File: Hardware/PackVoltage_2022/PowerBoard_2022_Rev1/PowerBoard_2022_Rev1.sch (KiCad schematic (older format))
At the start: 0 parts

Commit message: 12V stuff and hierarchical tags
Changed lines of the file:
@@
 $Descr A4 11693 8268
 encoding utf-8
-Sheet 1 8
+Sheet 1 10
 Title ""
 Date ""
@@
 $EndDescr
 $Sheet
-S 9350 850  1350 1100
+S 9750 650  1350 1100
 U 61563C60
 F0 "Bucks" 50
 F1 "Bucks.sch" 50
-F2 "PV" I L 9350 900 50
-F3 "5V" I L 9350 1000 50
-F4 "3.3V" I L 9350 1100 50
-F5 "12V" I L 9350 1200 50
-F6 "12VA" I L 9350 1300 50
+F2 "PV" I L 9750 700 50
+F3 "5V" I L 9750 800 50
+F4 "3.3V" I L 9750 900 50
+F5 "12V" I L 9750 1000 50
+F6 "12VA" I L 9750 1100 50
 $EndSheet
 $Sheet
@@
 $EndSheet
 $Sheet
-S 4800 3700 2650 2100
+S 4750 3700 2650 2100
 U 615E92DD
 F0 "ANDERSONS" 50
 F1 "andersons.sch" 50
-F2 "Anderson_M2" I L 4800 3900 50
-F3 "Anderson_M1" I L 4800 3800 50
-F4 "Anderson_M3" I L 4800 4000 50
-F5 "Anderson_M4" I L 4800 4100 50
-F6 "Anderson_M5" I L 4800 4200 50
-F7 "Anderson_M6" I L 4800 4300 50
-F8 "Anderson_M7" I L 4800 4400 50
+F2 "Anderson_M2" I L 4750 3900 50
+F3 "Anderson_M1" I L 4750 3800 50
+F4 "Anderson_M3" I L 4750 4000 50
+F5 "Anderson_M4" I L 4750 4100 50
+F6 "Anderson_M5" I L 4750 4200 50
+F7 "Anderson_M6" I L 4750 4300 50
+F8 "Anderson_M7" I L 4750 4400 50
+F9 "Anderson_Drive" I L 4750 4500 50
+F10 "Anderson_Aux" I L 4750 4600 50
+F11 "Anderson_Multimedia" I L 4750 4700 50
+F12 "Anderson_SciHeater" I L 4750 4800 50
+F13 "Anderson_POE" I L 4750 4900 50
+F14 "Anderson_SciSensor" I R 7400 3800 50
+F15 "Anderson_BBB" I R 7400 3900 50
+F16 "Anderson_Nav" I R 7400 4000 50
+F17 "Anderson_Cam1" I R 7400 4100 50
+F18 "Anderson_Cam2" I R 7400 4200 50
+F19 "Anderson_Gimbal" I R 7400 4300 50
+F20 "Anderson_NetSwitch" I R 7400 4400 50
 $EndSheet
 $Sheet
-S 1450 3650 2600 2100
+S 850  5200 1450 1450
 U 615D5992
 F0 "MOTORS" 50
 F1 "MOTORS.sch" 50
-F2 "PV" I L 1450 3700 50
-F3 "5V" I L 1450 3800 50
-F4 "Anderson_M1" I L 1450 4900 50
-F5 "Driver_M1" I R 4050 3750 50
-F6 "Current_Sensor_M1" I R 4050 4900 50
+F2 "PV" I L 850 5250 50
+F3 "5V" I L 850 5350 50
+F4 "Anderson_M1" I L 850 6550 50
+F5 "Driver_M1" I R 2300 5250 50
+F6 "Current_Sensor_M1" I R 2300 6550 50
+F7 "Anderson_M2" I L 850 6450 50
+F8 "Driver_M2" I R 2300 5350 50
+F9 "Current_Sensor_M2" I R 2300 6450 50
+F10 "Anderson_M3" I L 850 6350 50
+F11 "Driver_M3" I R 2300 5450 50
+F12 "Current_Sensor_M3" I R 2300 6350 50
+F13 "Anderson_M4" I L 850 6250 50
+F14 "Driver_M4" I R 2300 5550 50
+F15 "Current_Sensor_M4" I R 2300 6250 50
+F16 "Anderson_M5" I L 850 6150 50
+F17 "Driver_M5" I R 2300 5650 50
+F18 "Current_Sensor_M5" I R 2300 6150 50
+F19 "Anderson_M7" I L 850 5950 50
+F20 "Driver_M7" I R 2300 5850 50
+F21 "Current_Sensor_M7" I R 2300 5950 50
+F22 "Anderson_M6" I L 850 6050 50
+F23 "Driver_M6" I R 2300 5750 50
+F24 "Current_Sensor_M6" I R 2300 6050 50
 $EndSheet
 $Sheet
-S 4800 1150 2850 2200
+S 4850 1000 2850 2200
 U 615D7BA0
 F0 "12V" 50
 F1 "12V.sch" 50
+F2 "Anderson_Aux" I L 4850 1100 50
+F3 "PV" I R 7700 1050 50
+F4 "5V" I R 7700 1150 50
+F5 "Anderson_Spare" I L 4850 1200 50
+F6 "Anderson_Nav" I L 4850 1300 50
+F7 "Anderson_SciSensor" I L 4850 1400 50
+F8 "Anderson_BBB" I L 4850 1500 50
+F9 "Anderson_Cam1" I L 4850 1600 50
+F10 "Anderson_Cam2" I L 4850 1700 50
+F11 "Anderson_NetSwitch" I L 4850 1800 50
+F12 "Anderson_Gimbal" I L 4850 1900 50
+F13 "12V" I R 7700 1250 50
+F14 "Driver_Nav" I R 7700 2350 50
+F15 "Driver_SciSensor" I R 7700 2450 50
+F16 "Driver_BBB" I R 7700 2550 50
+F17 "Driver_Cam1" I R 7700 2650 50
+F18 "Driver_Cam2" I R 7700 2750 50
+F19 "Driver_NetSwitch" I R 7700 2850 50
+F20 "Driver_Gimbal" I R 7700 2950 50
+F21 "Driver_Aux" I R 7700 3050 50
+F22 "Driver_Spare" I R 7700 3150 50
+F23 "Current_Sensor_BBB" I L 4850 2350 50
+F24 "Current_Sensor_Nav" I L 4850 2450 50
+F25 "Current_Sensor_SciSensor" I L 4850 2550 50
+F26 "Current_Sensor_Cam1" I L 4850 2650 50
+F27 "Current_Sensor_Cam2" I L 4850 2750 50
+F28 "Current_Sensor_NetSwitch" I L 4850 2850 50
+F29 "Current_Sensor_Gimbal" I L 4850 2950 50
+F30 "Current_Sensor_Aux" I L 4850 3050 50
+F31 "Current_Sensor_Spare" I L 4850 3150 50
 $EndSheet
+$Sheet
+S 2400 3700 2050 1350
+U 61609A41
+F0 "PACK_OTHERS" 50
+F1 "PACK_OTHERS.sch" 50
+F2 "PV" I L 2400 3750 50
+F3 "5V" I L 2400 3850 50
+F4 "Anderson_Drive" I L 2400 4950 50
+F5 "Driver_Drive" I R 4450 3800 50
+F6 "Current_Sensor_Drive" I R 4450 4950 50
+F7 "Anderson_Aux" I L 2400 4850 50
+F8 "Driver_Aux" I R 4450 3900 50
+F9 "Current_Sensor_Aux" I R 4450 4850 50
+F10 "Anderson_SciHeater" I L 2400 4750 50
+F11 "Driver_SciHeater" I R 4450 4000 50
+F12 "Current_Sensor_SciHeater" I R 4450 4750 50
+F13 "Anderson_Multimedia" I L 2400 4650 50
+F14 "Driver_Multimedia" I R 4450 4100 50
+F15 "Current_Sensor_Multimedia" I R 4450 4650 50
+F16 "Anderson_POE" I L 2400 4550 50
+F17 "Driver_POE" I R 4450 4200 50
+F18 "Current_Sensor_POE" I R 4450 4550 50
+$EndSheet
+Text GLabel 9650 700  0    50   Input ~ 0
+PV
+Wire Wire Line
+	9650 700  9750 700
+Text GLabel 7800 1050 2    50   Input ~ 0
+PV
+Wire Wire Line
+	7800 1050 7700 1050
+Text GLabel 2300 3750 0    50   Input ~ 0
+PV
+Wire Wire Line
+	2300 3750 2400 3750
+Text GLabel 750  5250 0    50   Input ~ 0
+PV
+Wire Wire Line
+	750  5250 850  5250
 $EndSCHEMATC

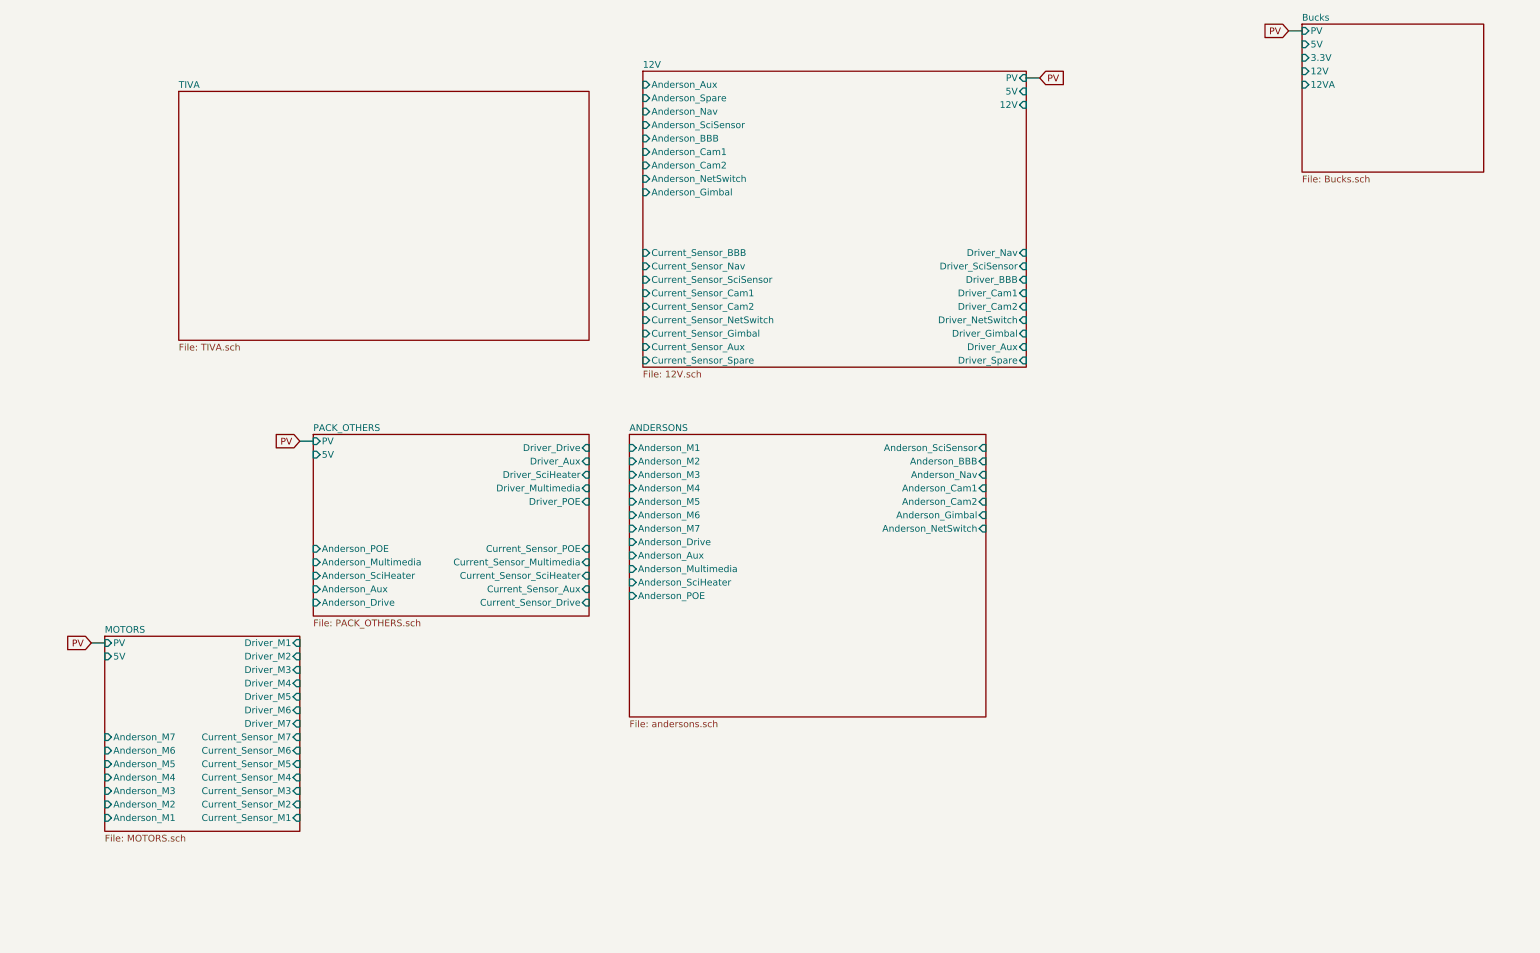
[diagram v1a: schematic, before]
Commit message: Created global tags in main sheet
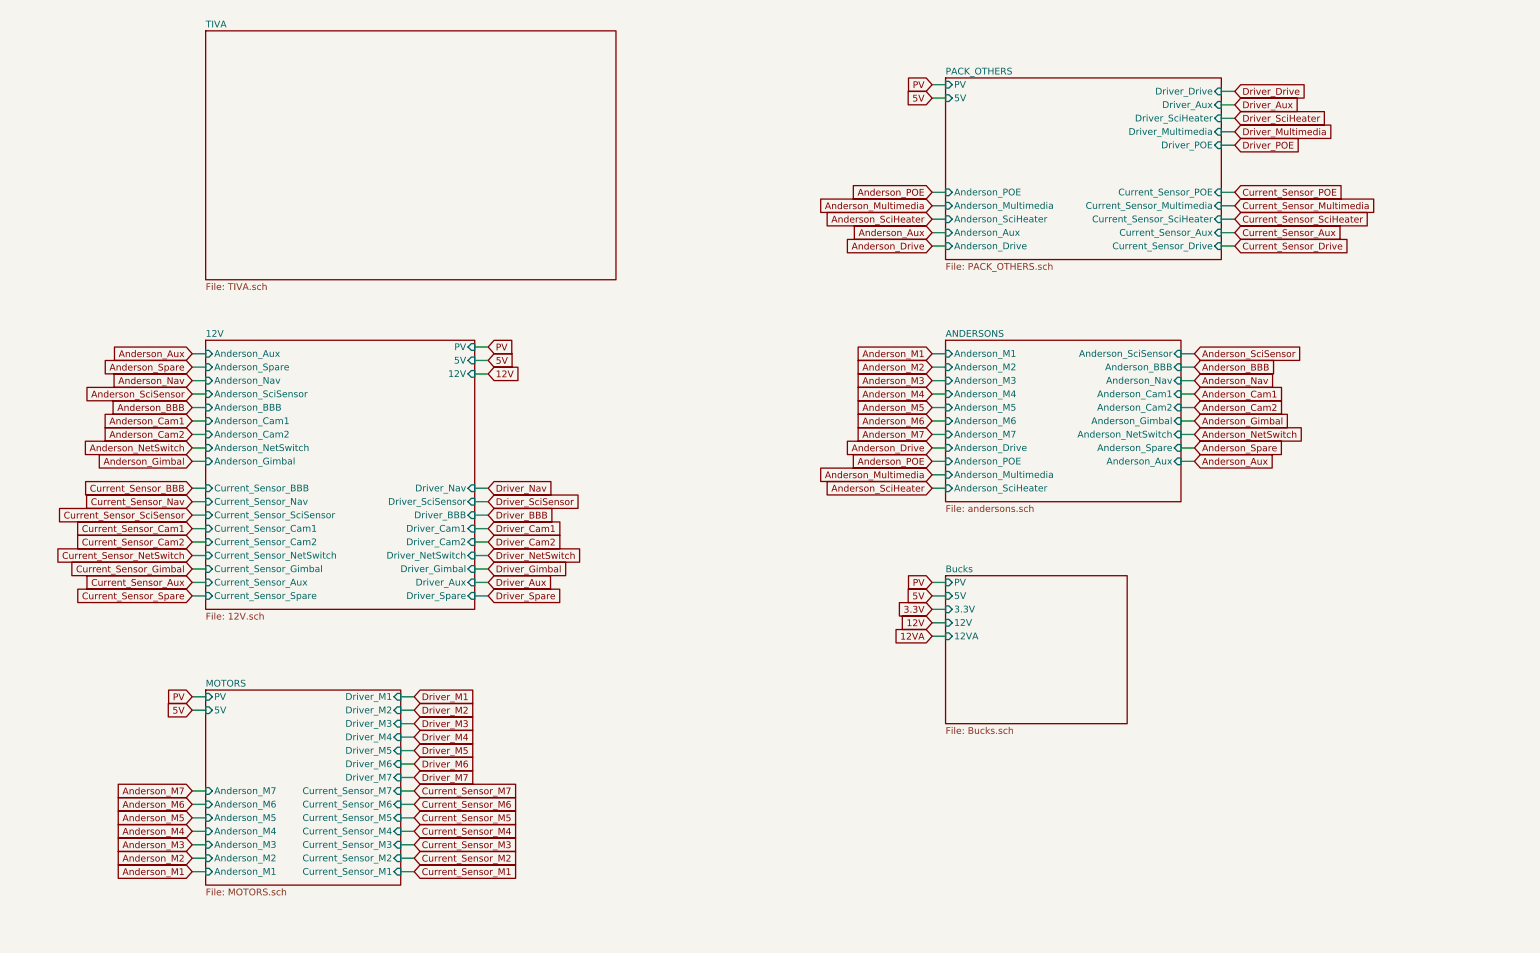
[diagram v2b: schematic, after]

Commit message: TIVA and fixed 12V
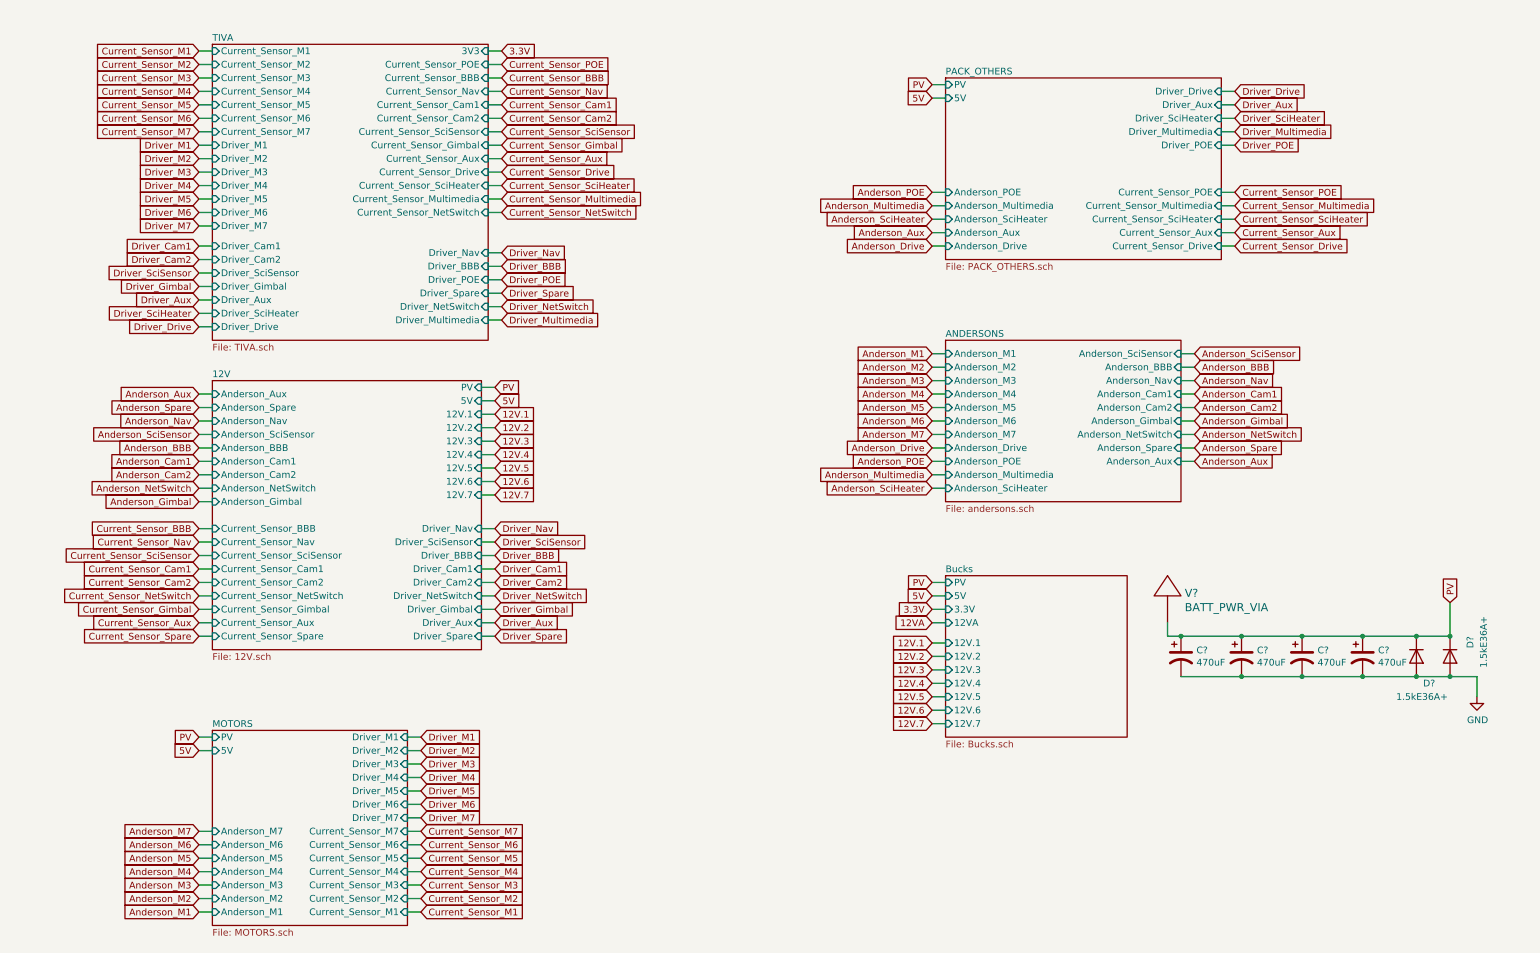
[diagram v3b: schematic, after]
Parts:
- added C? (x4): 470uF, symbol Device:CP1
- added D? (x2): 1.5kE36A+, symbol Device:D
- added V?: BATT_PWR_VIA, symbol MRDT_Drill_Holes:BATT_PWR_VIA
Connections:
- net PV: now also C?.1, C?.1, C?.1, C?.1, D?.1 (K), D?.1 (K), V?.1
- new net GND: C?.2, C?.2, C?.2, C?.2, D?.2 (A), D?.2 (A)

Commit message: Fixed some stuff
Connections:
- net labels added: 12VBBB, 12VCam1, 12VCam2, 12VDrive, 12VGimbal, 12VMultimedia, 12VNav, 12VNetSwitch, 12VSciSensor
- net labels removed: 12V.1, 12V.2, 12V.3, 12V.4, 12V.5, 12V.6, 12V.7
- wire segments 162 -> 160

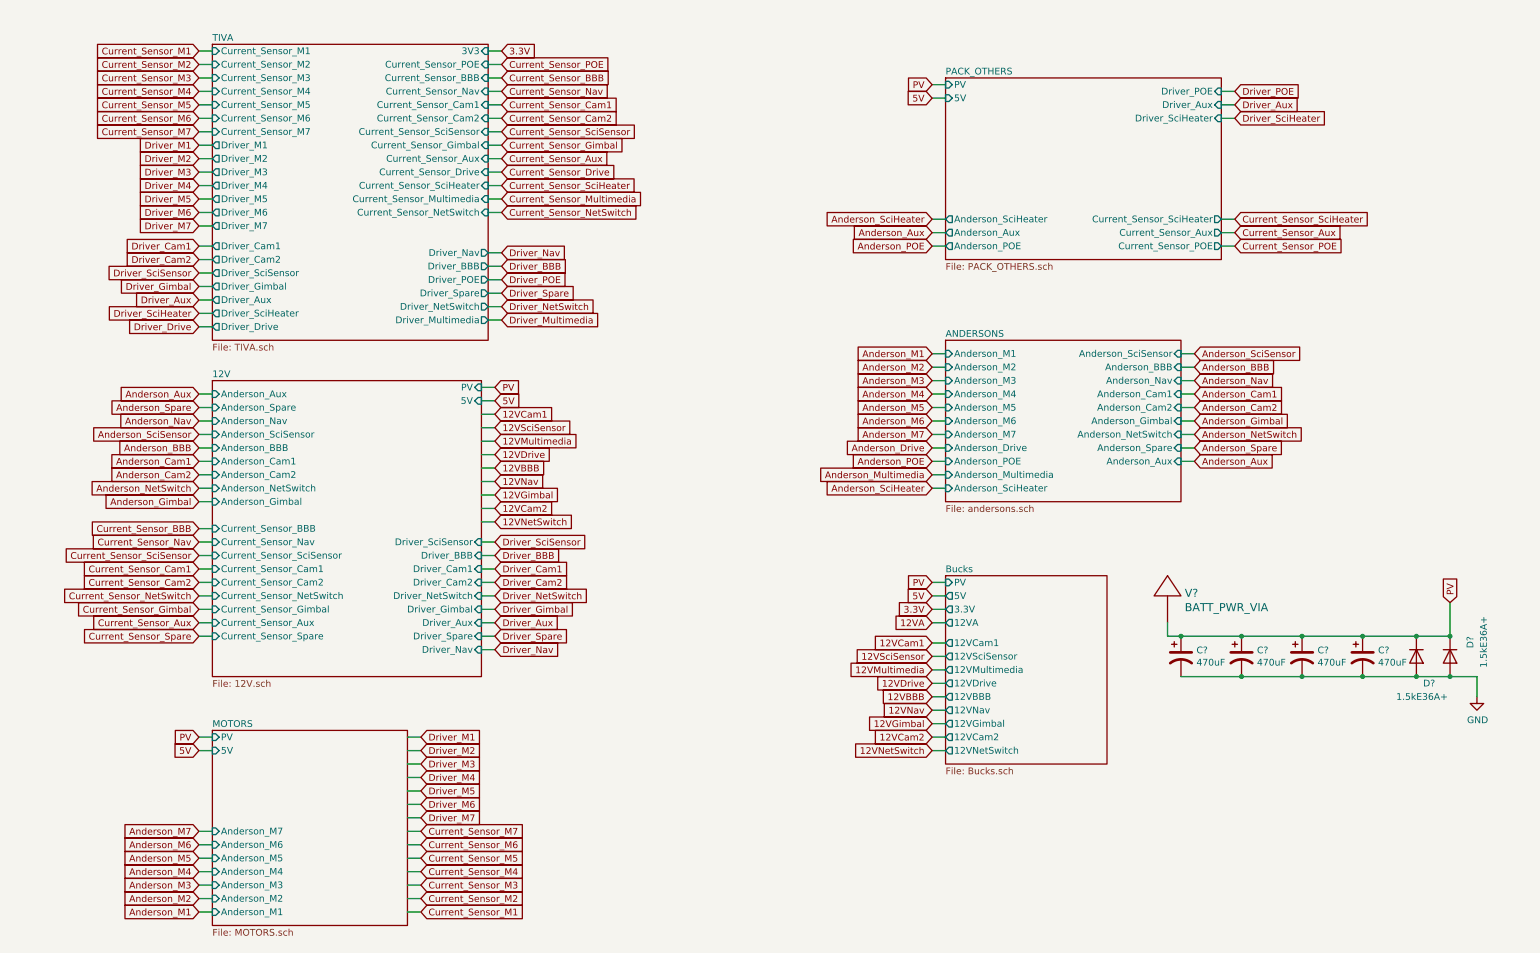
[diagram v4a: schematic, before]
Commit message: Changed values of LED resistors, changed some of the outputs to inputs, and made board look better
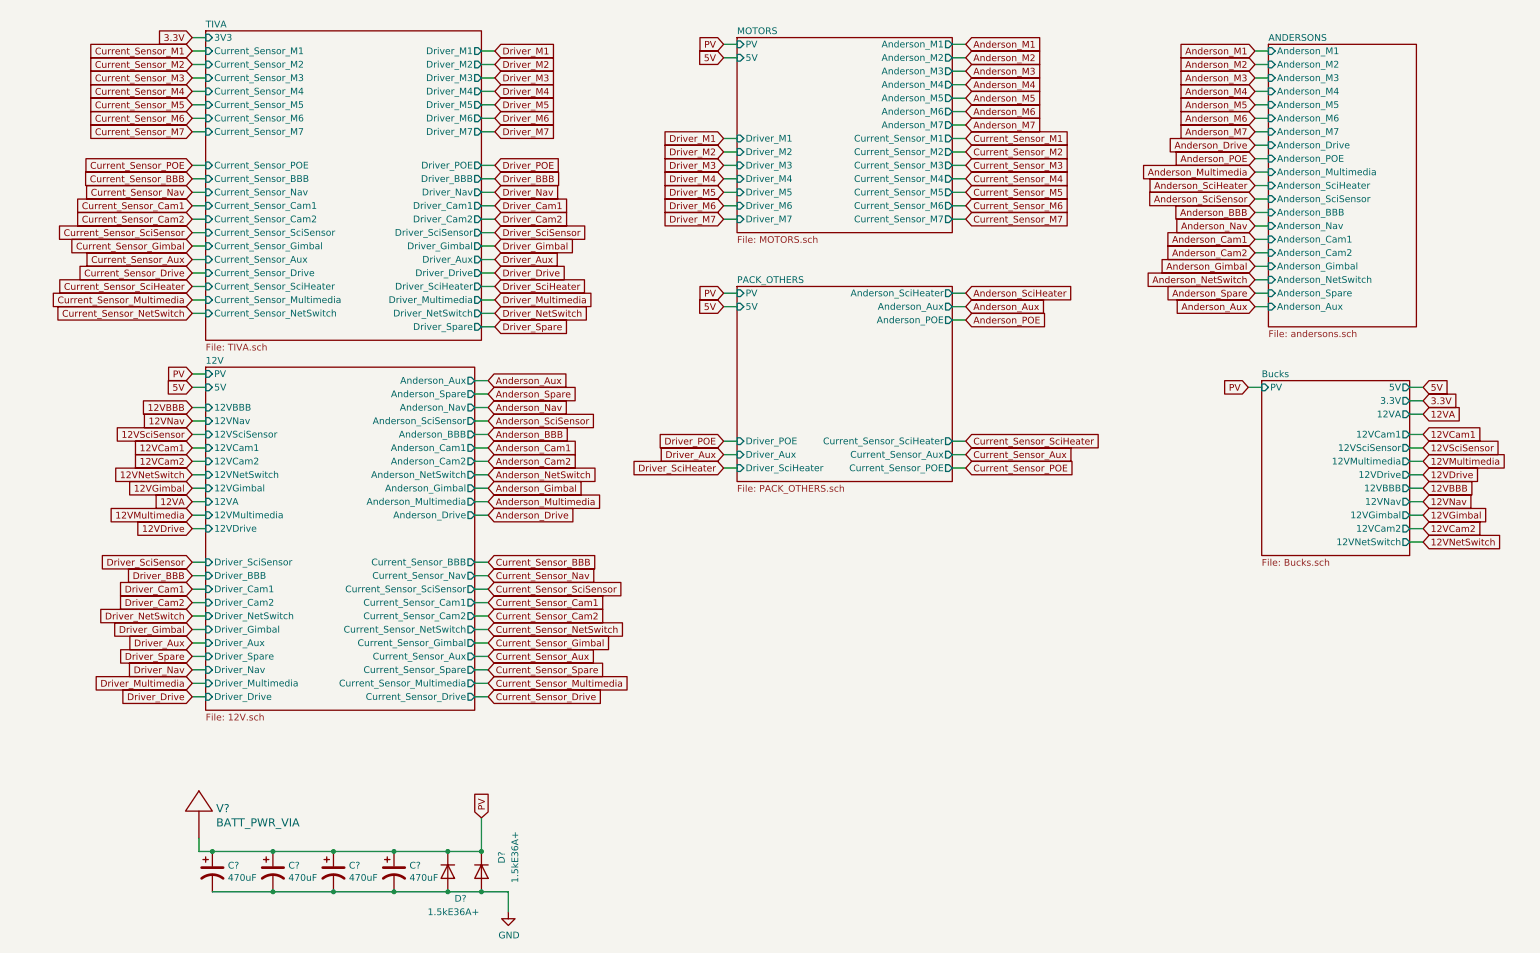
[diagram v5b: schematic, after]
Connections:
- wire segments 160 -> 167
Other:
- moved on the sheet: C?, D?, V?
